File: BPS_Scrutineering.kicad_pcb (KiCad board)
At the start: 2 copper layers, 87.9 x 87.4 mm, 22 parts, among them J1 Conn_01x01_Female, J10 Conn_01x01_Female, J11 Conn_01x01_Female, J12 Conn_01x01_Female, J13 Conn_01x01_Female, J14 Conn_01x01_Female, J2 Conn_01x01_Female, J3 Conn_01x01_Female, J4 Conn_01x01_Female, J5 Conn_01x01_Female, J6 Conn_01x01_Female, J7 Conn_01x01_Female, J8 Conn_01x01_Female, J9 Conn_01x01_Female, SW1 SW_DIP_x07, SW2 SW_DIP_x07

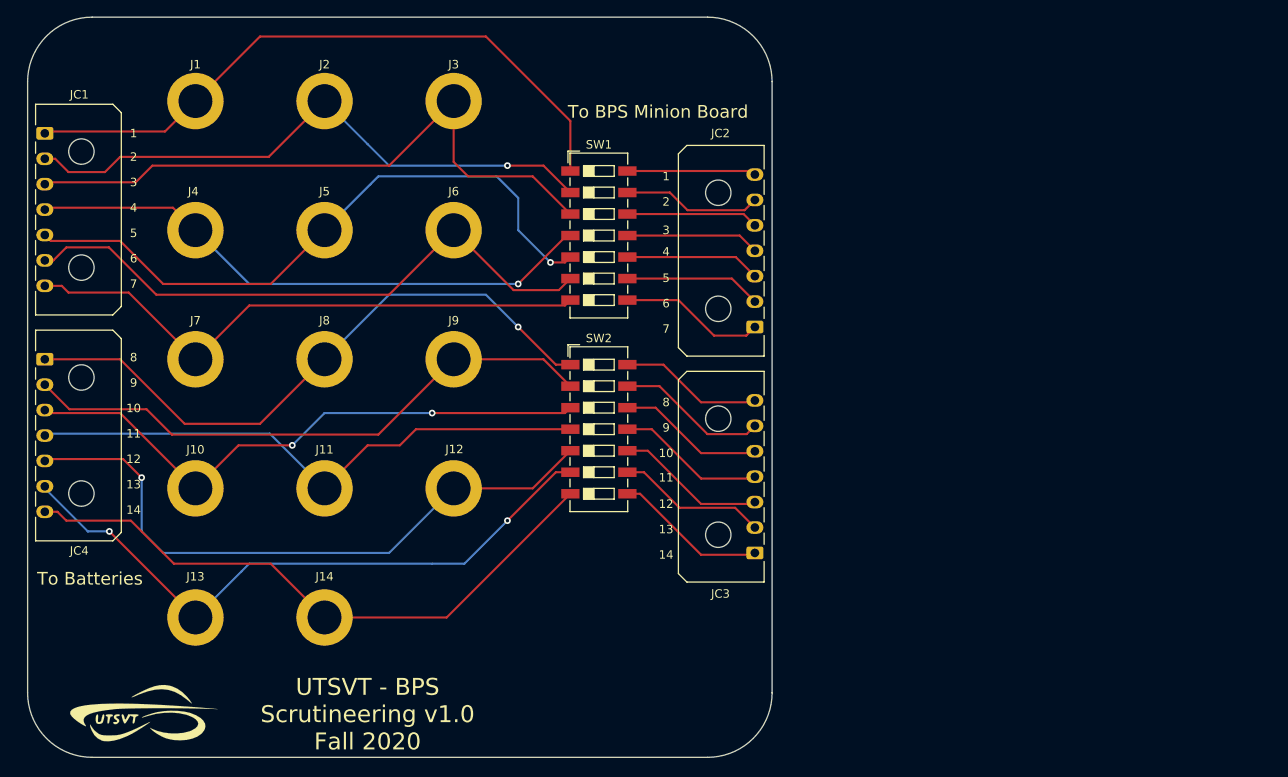
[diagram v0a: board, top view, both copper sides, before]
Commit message: new jacks, redid traces, fixed Hannah's comments
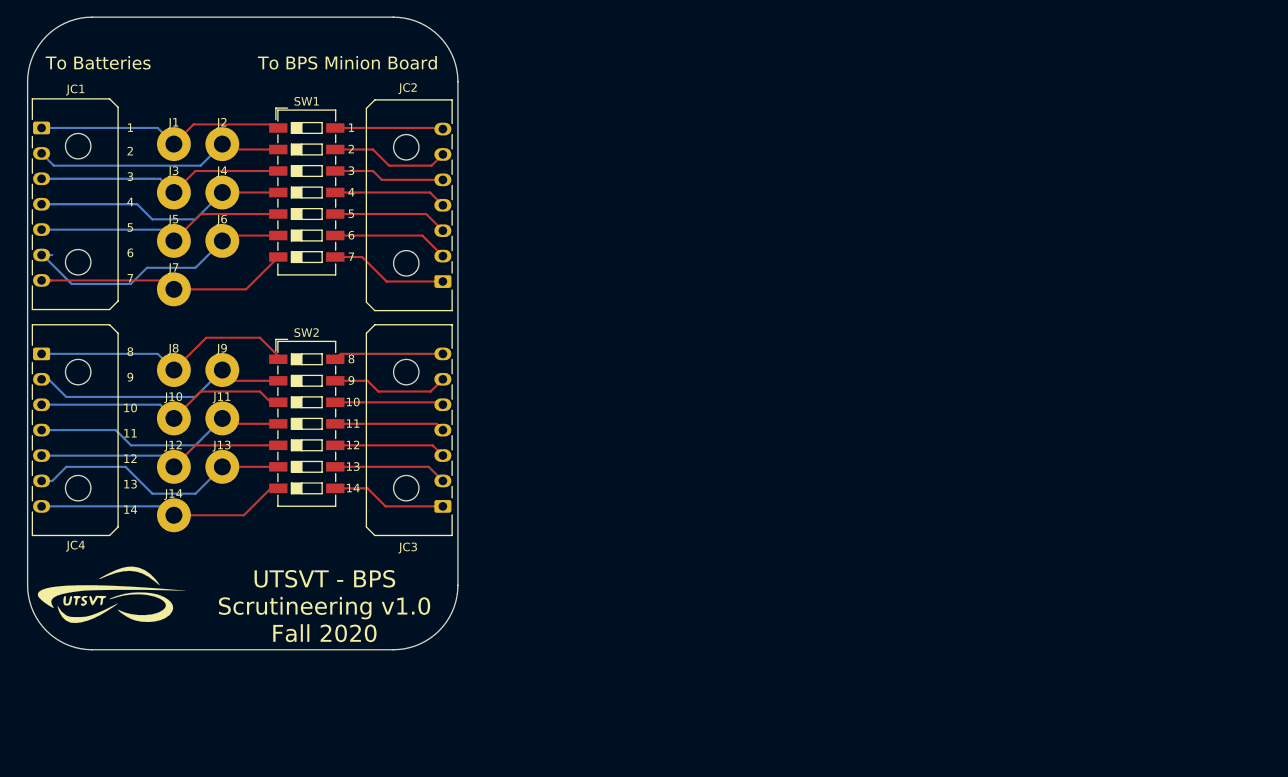
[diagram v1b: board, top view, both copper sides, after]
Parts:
- moved Dr_Hallock1 49.3 mm to (98.0, 80.3)
- moved JC3 37.2 mm to (120.7, 99.9)
- moved JC2 37.2 mm to (120.7, 73.4)
- moved SW1 34.9 mm to (104.6, 62.9)
- moved SW2 34.5 mm to (104.6, 90.2)
- moved J3 34.0 mm to (88.9, 60.3)
- moved J12 33.4 mm to (88.9, 92.7)
- moved J6 27.3 mm to (94.6, 66.0)
- moved J9 27.3 mm to (94.6, 81.3)
- moved J14 23.0 mm to (88.9, 98.4)
- moved J13 20.6 mm to (94.6, 92.7)
- moved J5 17.8 mm to (88.9, 66.0)
- moved J8 17.8 mm to (88.9, 81.3)
- moved J11 16.2 mm to (94.6, 87.0)
- moved UTSVT_Logo1 14.5 mm to (81.3, 110.5)
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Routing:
- net Net-(J1-Pad1): track 76.8 -> 29.9 mm
- net Net-(J5-Pad1): track 76.4 -> 29.8 mm, vias 1 -> 0
- net Net-(J12-Pad1): track 75.4 -> 29.5 mm, vias 1 -> 0
- net Net-(J3-Pad1): track 75.8 -> 30.0 mm
- net Net-(J13-Pad1): track 75.7 -> 31.5 mm, vias 2 -> 0
- net Net-(J14-Pad1): track 73.6 -> 30.0 mm
- net Net-(J8-Pad1): track 74.9 -> 31.6 mm, vias 1 -> 0
- net Net-(J2-Pad1): track 70.6 -> 29.9 mm, vias 1 -> 0
- net Net-(J10-Pad1): track 69.8 -> 30.9 mm, vias 2 -> 0
- net Net-(J9-Pad1): track 69.5 -> 30.6 mm
- net Net-(J6-Pad1): track 71.6 -> 33.0 mm
- net Net-(J4-Pad1): track 68.2 -> 30.3 mm, vias 1 -> 0
- net Net-(J7-Pad1): track 68.8 -> 31.2 mm
- net Net-(J11-Pad1): track 67.7 -> 30.3 mm
- net Net-(JC3-Pad2): track 17.8 -> 13.4 mm
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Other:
- board size 87.9 x 87.4 mm -> 50.8 x 74.7 mm
- board text removed: "J1"
- board text removed: "J10"
- board text removed: "J11"
- board text removed: "J12"
- board text removed: "J13"
- board text removed: "J14"
- board text removed: "J2"
- board text removed: "J3"
- board text removed: "J4"
- board text removed: "J5"
- board text removed: "J6"
- board text removed: "J7"
- board text removed: "J8"
- board text removed: "J9"

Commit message: Fix issues with connector sizes and wiring
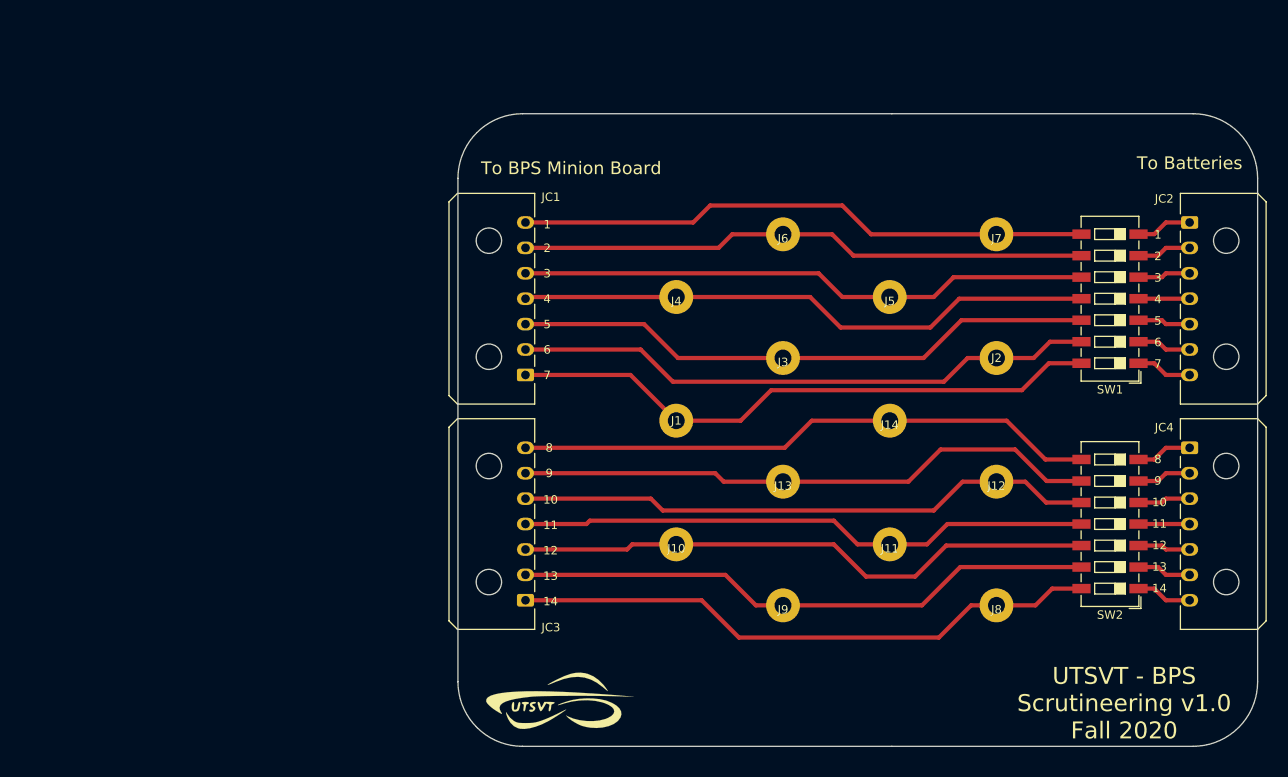
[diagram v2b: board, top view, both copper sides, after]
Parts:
- moved J8 101.7 mm to (186.0, 111.6)
- moved J12 97.2 mm to (186.0, 97.0)
- moved J7 97.2 mm to (186.0, 67.8)
- moved SW1 95.6 mm to (199.4, 75.4), turned to 180 degrees
- moved SW2 95.6 mm to (199.4, 102.0), turned to 180 degrees
- moved J2 95.5 mm to (186.0, 82.4)
- moved JC2 88.4 mm to (208.8, 66.4), turned to 270 degrees
- moved JC4 88.4 mm to (208.8, 93.0), turned to 270 degrees
- moved J5 85.0 mm to (173.4, 75.2)
- moved J14 84.9 mm to (173.4, 89.8)
- moved J11 80.7 mm to (173.4, 104.4)
- moved J3 75.2 mm to (160.8, 82.4)
- moved J9 72.8 mm to (160.8, 111.6)
- moved J1 69.0 mm to (148.2, 89.8)
- moved J13 66.3 mm to (160.8, 97.0)
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- renumbered JC4 to JC3, JC3 to JC4
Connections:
- JC4 pad 1: Net-(JC3-Pad1) -> Net-(JC4-Pad1)
- JC4 pad 2: Net-(JC3-Pad2) -> Net-(JC4-Pad2)
- JC4 pad 3: Net-(JC3-Pad3) -> Net-(JC4-Pad3)
- JC4 pad 4: Net-(JC3-Pad4) -> Net-(JC4-Pad4)
- JC4 pad 5: Net-(JC3-Pad5) -> Net-(JC4-Pad5)
- JC4 pad 6: Net-(JC3-Pad6) -> Net-(JC4-Pad6)
- JC4 pad 7: Net-(JC3-Pad7) -> Net-(JC4-Pad7)
- SW1 pad 1: Net-(J1-Pad1) -> Net-(JC2-Pad7)
- SW1 pad 10: Net-(JC2-Pad3) -> Net-(J5-Pad1)
- SW1 pad 11: Net-(JC2-Pad4) -> Net-(J4-Pad1)
- SW1 pad 12: Net-(JC2-Pad5) -> Net-(J3-Pad1)
- SW1 pad 13: Net-(JC2-Pad6) -> Net-(J2-Pad1)
- SW1 pad 14: Net-(JC2-Pad7) -> Net-(J1-Pad1)
- SW1 pad 2: Net-(J2-Pad1) -> Net-(JC2-Pad6)
- SW1 pad 3: Net-(J3-Pad1) -> Net-(JC2-Pad5)
- SW1 pad 4: Net-(J4-Pad1) -> Net-(JC2-Pad4)
- SW1 pad 5: Net-(J5-Pad1) -> Net-(JC2-Pad3)
- SW1 pad 6: Net-(J6-Pad1) -> Net-(JC2-Pad2)
- SW1 pad 7: Net-(J7-Pad1) -> Net-(JC2-Pad1)
- SW1 pad 8: Net-(JC2-Pad1) -> Net-(J7-Pad1)
- SW1 pad 9: Net-(JC2-Pad2) -> Net-(J6-Pad1)
- SW2 pad 1: Net-(J8-Pad1) -> Net-(JC4-Pad7)
- SW2 pad 10: Net-(JC3-Pad3) -> Net-(J12-Pad1)
- SW2 pad 11: Net-(JC3-Pad4) -> Net-(J11-Pad1)
- SW2 pad 12: Net-(JC3-Pad5) -> Net-(J10-Pad1)
- SW2 pad 13: Net-(JC3-Pad6) -> Net-(J9-Pad1)
- SW2 pad 14: Net-(JC3-Pad7) -> Net-(J8-Pad1)
- SW2 pad 2: Net-(J9-Pad1) -> Net-(JC4-Pad6)
- SW2 pad 3: Net-(J10-Pad1) -> Net-(JC4-Pad5)
- SW2 pad 4: Net-(J11-Pad1) -> Net-(JC4-Pad4)
- SW2 pad 5: Net-(J12-Pad1) -> Net-(JC4-Pad3)
- SW2 pad 6: Net-(J13-Pad1) -> Net-(JC4-Pad2)
- SW2 pad 7: Net-(J14-Pad1) -> Net-(JC4-Pad1)
- SW2 pad 8: Net-(JC3-Pad1) -> Net-(J14-Pad1)
- SW2 pad 9: Net-(JC3-Pad2) -> Net-(J13-Pad1)
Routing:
- net Net-(J1-Pad1): track 29.9 -> 70.7 mm
- net Net-(J2-Pad1): track 29.9 -> 69.2 mm
- net Net-(J3-Pad1): track 30.0 -> 69.1 mm
- net Net-(J12-Pad1): track 29.5 -> 68.6 mm
- net Net-(J14-Pad1): track 30.0 -> 68.9 mm
- net Net-(J9-Pad1): track 30.6 -> 69.0 mm
- net Net-(J4-Pad1): track 30.3 -> 68.6 mm
- net Net-(J8-Pad1): track 31.6 -> 69.9 mm
- net Net-(J10-Pad1): track 30.9 -> 69.0 mm
- net Net-(J5-Pad1): track 29.8 -> 67.8 mm
- net Net-(J11-Pad1): track 30.3 -> 68.0 mm
- net Net-(J13-Pad1): track 31.5 -> 69.2 mm
- net Net-(J7-Pad1): track 31.2 -> 67.9 mm
- net Net-(J6-Pad1): track 33.0 -> 67.3 mm
- net Net-(JC3-Pad1): track 13.9 -> 0.00 mm
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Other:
- board size 50.8 x 74.7 mm -> 94.4 x 74.7 mm

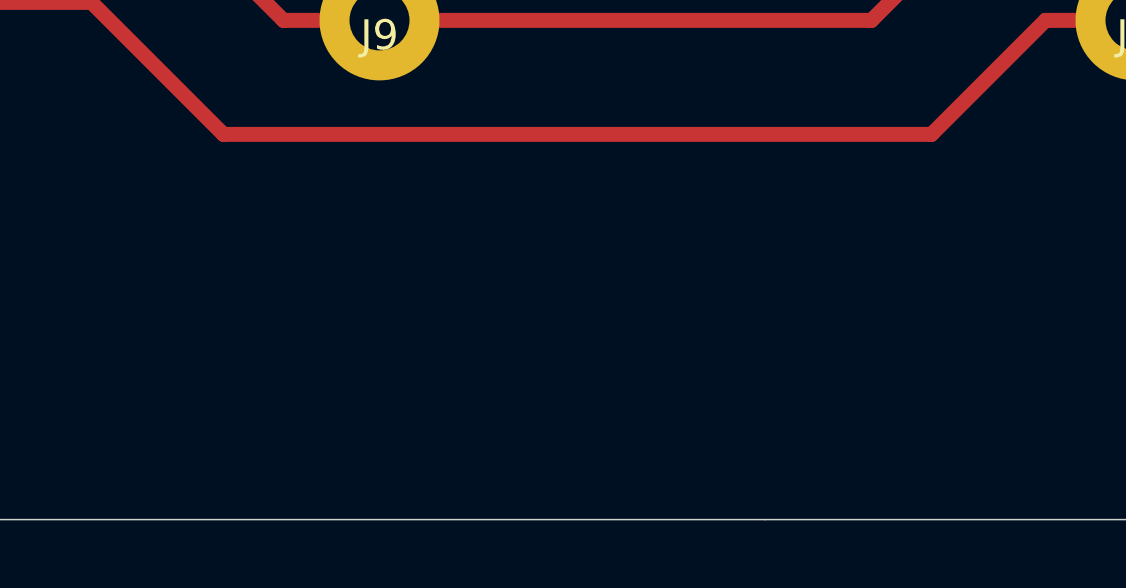
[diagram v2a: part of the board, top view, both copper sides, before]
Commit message: Add banana connector key to the board
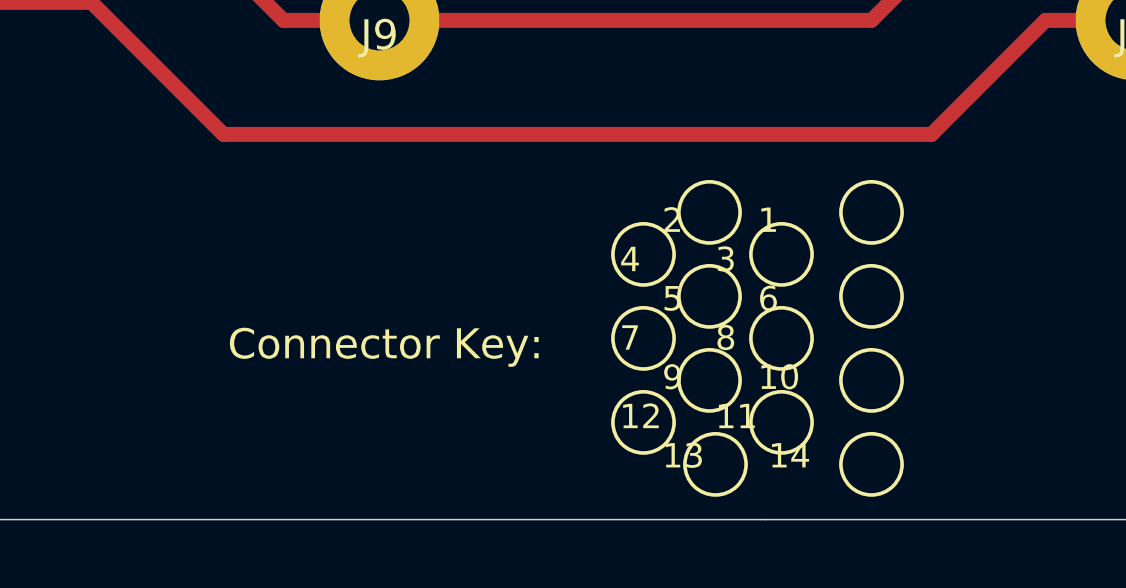
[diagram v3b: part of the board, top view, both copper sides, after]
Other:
- board text added: "2 1 4 3 5 6 7 8 9 10 12 11 13 14"
- board text added: "Connector Key:"

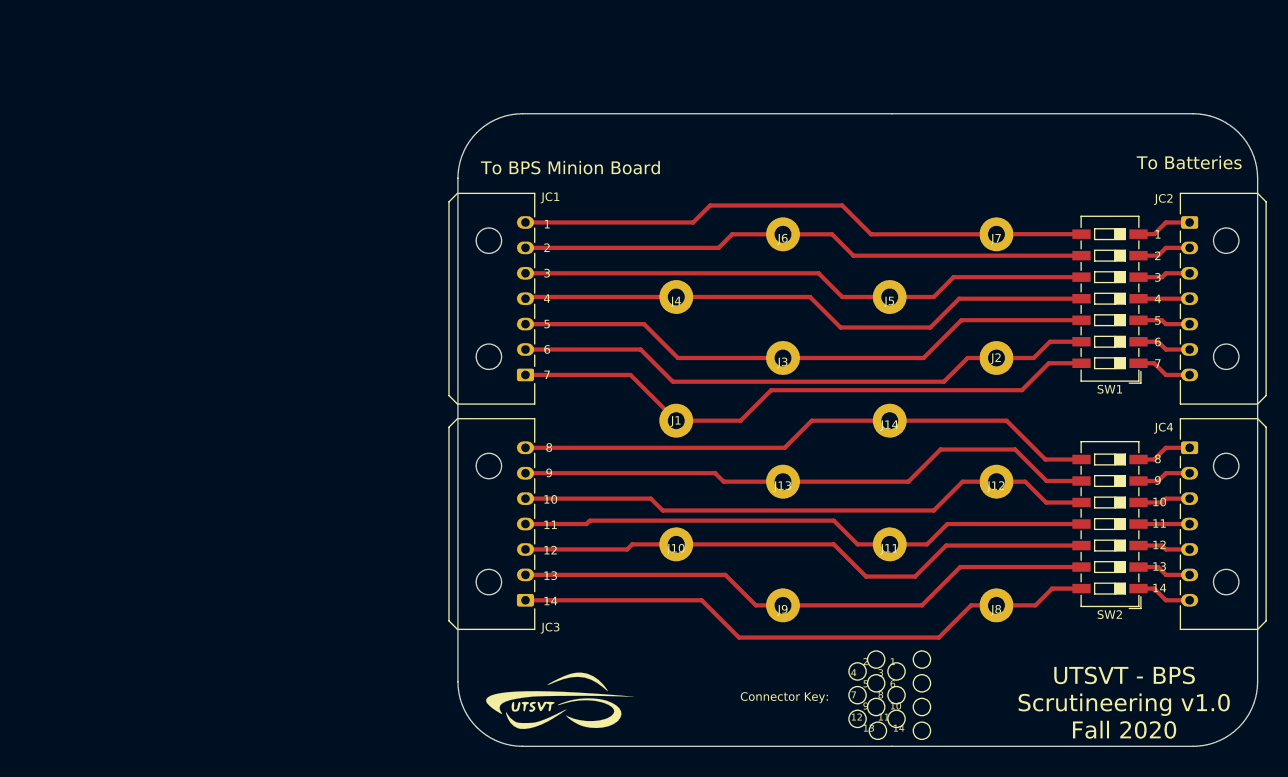
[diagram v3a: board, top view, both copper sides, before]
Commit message: Adds names and adds labels to logos on schematic
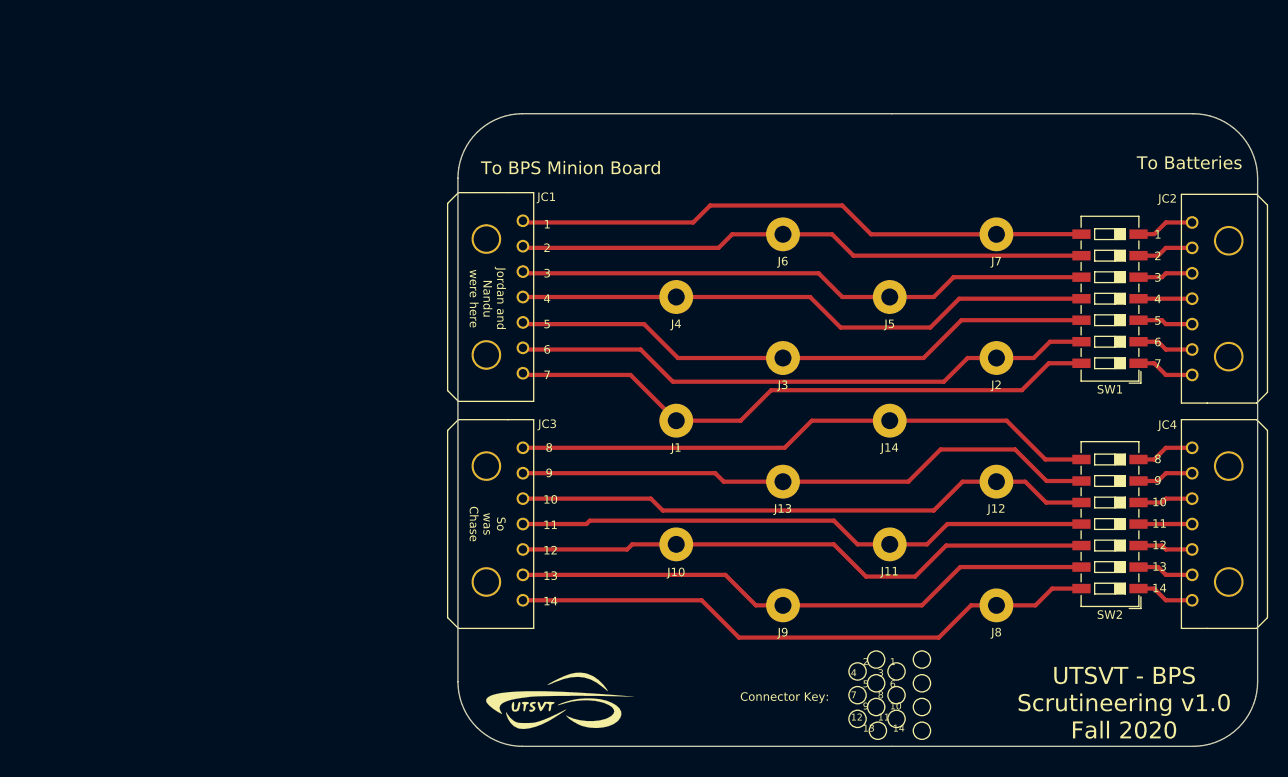
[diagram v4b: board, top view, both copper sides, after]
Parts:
- Dr_Hallock1: value Logo_Placeholder -> Dr. Hallock
- JC1, JC2, JC3, JC4: footprint Connector_Molex:Molex_Micro-Fit_3.0_43650-0700_1x07_P3.00mm_Horizontal -> UTSVT_Connectors:Molex_MicroFit_01x07_Horizontal
- UTSVT_Logo1: value Logo_Placeholder -> UTSVT
- moved JC1 9.20 mm to (130.1, 75.2), turned to 270 degrees
- moved JC3 9.00 mm to (130.1, 102.0), turned to 270 degrees
- moved JC2 9.00 mm to (209.1, 75.4), turned to 90 degrees
- moved JC4 9.00 mm to (209.1, 102.0), turned to 90 degrees
- moved Dr_Hallock1 5.18 mm to (140.1, 106.5)
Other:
- board text added: "Dr. Gary Hallock"
- board text added: "Jordan and Nandu were here"
- board text added: "So was Chase"
